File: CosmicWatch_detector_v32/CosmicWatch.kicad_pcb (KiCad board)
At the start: 2 copper layers, 99.9 x 100 mm, 95 parts, among them J3 RJ45, P1 CONN_01X04, P10 CONN_02X02, P11 CONN_01X01, P12 CONN_01X01, P13 CONN_01X01, P14 CONN_01X01, P15 CONN_02X04, P16 CONN_01X02, P19 CONN_01X01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

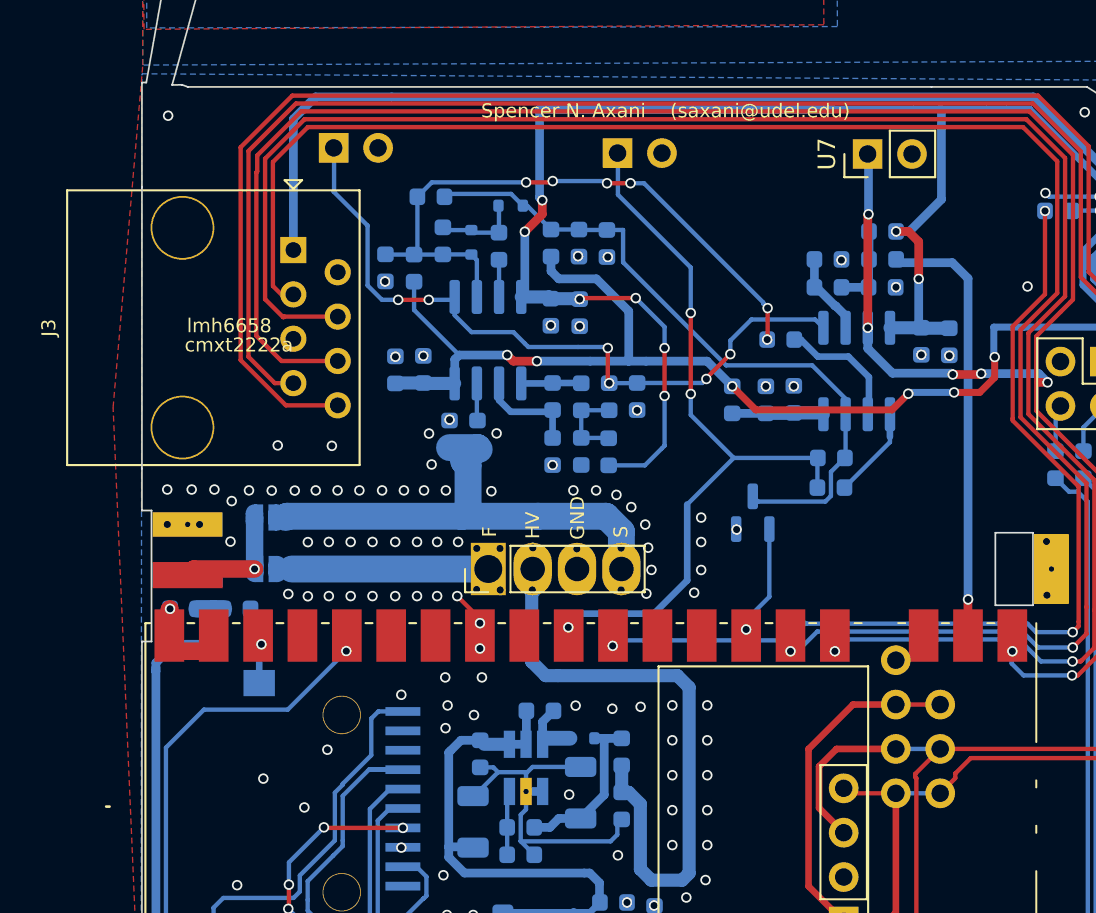
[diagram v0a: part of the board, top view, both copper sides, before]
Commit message: updating pcb
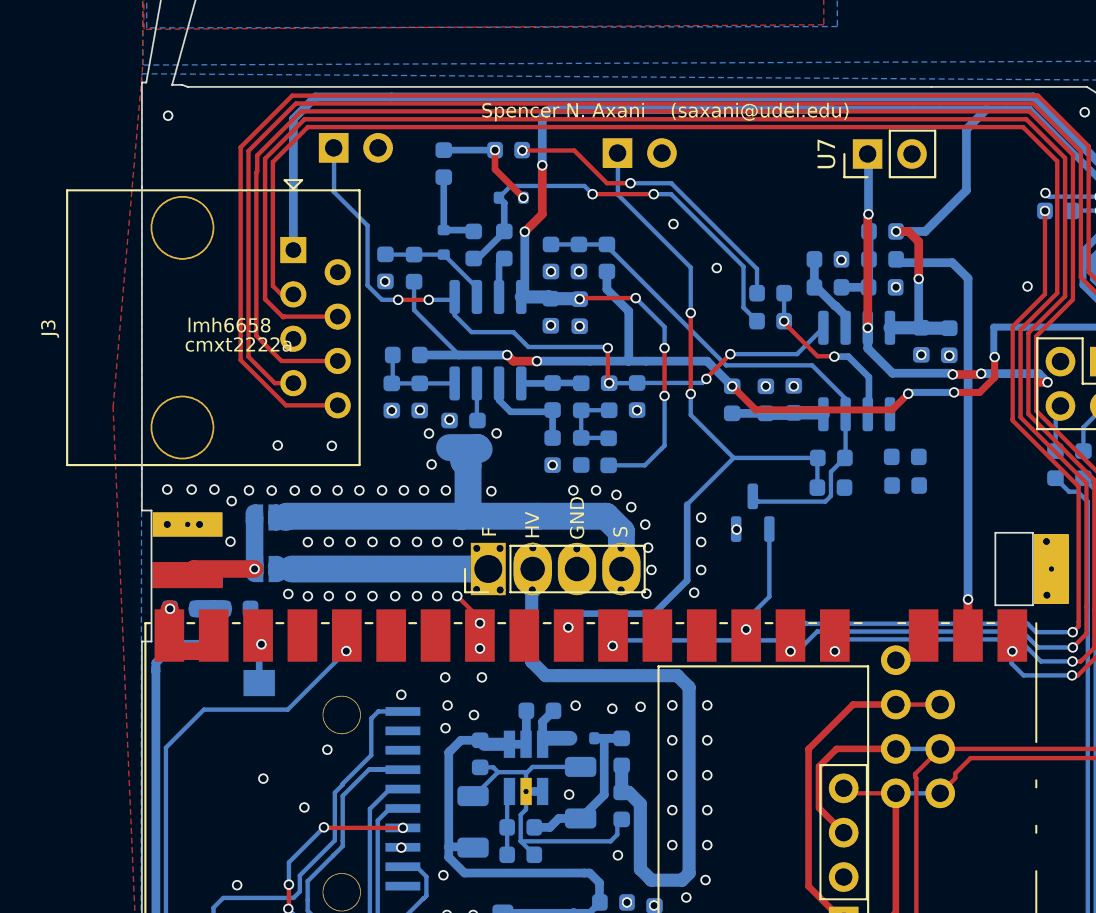
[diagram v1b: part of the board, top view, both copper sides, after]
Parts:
- removed C19: 1nF, Capacitor_SMD:C_0603_1608Metric
- added R28: 47k, Capacitor_SMD:C_0603_1608Metric, B.Cu at (76.7, 101.9)
- added R29: 0, Capacitor_SMD:C_0603_1608Metric, B.Cu at (80.5, 95.6)
- added R30: NA, Capacitor_SMD:C_0603_1608Metric, B.Cu at (78.8, 91.0)
- added R31: 100k, Capacitor_SMD:C_0603_1608Metric, B.Cu at (105.2, 107.8)
- added R32: NA, Capacitor_SMD:C_0603_1608Metric, B.Cu at (97.5, 100.0)
- added R34: 100k, Capacitor_SMD:C_0603_1608Metric, B.Cu at (105.2, 109.4)
- C21: value 0 -> 0.1uF
- R15, R19: value 100k -> NA
- R21: value 500 -> 0
- R23: value NA -> 47k
- R24: value 10k -> NA
- moved R24 5.19 mm to (82.5, 90.2)
- moved R19 3.31 mm to (88.1, 96.4), turned to -90 degrees
- moved R15 3.31 mm to (84.9, 96.4)
- moved R27 2.72 mm to (97.5, 98.4)
- moved C8 1.59 mm to (77.4, 104.3), turned to 90 degrees
- moved D5 1.58 mm to (78.8, 95.5), turned to -90 degrees
- moved C6 1.56 mm to (75.8, 104.3), turned to 90 degrees
- moved C25 0.86 mm to (86.5, 96.4)
- moved D3 0.46 mm to (82.7, 92.9)
- moved R21 0.31 mm to (82.3, 95.6)
- turned R23 to 90 degrees
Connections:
- C6 pad 2: VEE -> Net-(U6-V-)
- C8 pad 2: VEE -> Net-(U6-V-)
- D5 pad 2: Net-(D3-A) -> Net-(D5-A)
- R11 pad 2: SNG -> unconnected-(R11-Pad2)
- R14 pad 2: Net-(D5-K) -> Net-(D5-A)
- R19 pad 1: VEE -> PD
- R19 pad 2: PD -> VEE
- R23 pad 1: VEE -> Net-(U4-V-)
- R23 pad 2: Net-(U4-V-) -> VEE
- R24 pad 1: PD -> Net-(D5-A)
- R24 pad 2: Net-(D5-K) -> PD
- R26 pad 1: Net-(U4-OUTA) -> Net-(U4--INA)
- R27 pad 1: Net-(D5-K) -> Net-(D5-A)
- R9 pad 2: Net-(D5-K) -> Net-(D5-A)
- U4 pad 1: Net-(U4-OUTA) -> Net-(U4--INA)
- U6 pad 4: VEE -> Net-(U6-V-)
- U6 pad 6: Net-(D5-K) -> Net-(D5-A)
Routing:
- net Net-(D5-K): track 36.2 -> 4.98 mm, vias 6 -> 0
- net Net-(D5-A): track 0.00 -> 24.6 mm, vias 0 -> 2
- net Net-(D3-A): track 4.89 -> 24.2 mm, vias 0 -> 2
- net Net-(U4-OUTA): track 6.58 -> 0.00 mm
- net VEE: track 133.5 -> 127.2 mm
- net Net-(U6-V-): track 0.00 -> 5.25 mm
- net Net-(U4--INA): track 7.32 -> 10.00 mm, vias 0 -> 2
- net PD: track 39.6 -> 37.6 mm, vias 0 -> 2
- net VCC: track 201.2 -> 202.3 mm
- net AMP1: track 41.1 -> 40.2 mm
- net GNDA: vias 164 -> 166
